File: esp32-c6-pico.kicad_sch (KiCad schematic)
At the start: 52 parts, among them SW1 RESET, SW2 BOOT, U1 ESP32-C6, U3 W25Q32JVZPIQ, U4 SN74LV1T125, Y1 40MHz / CL=8pF

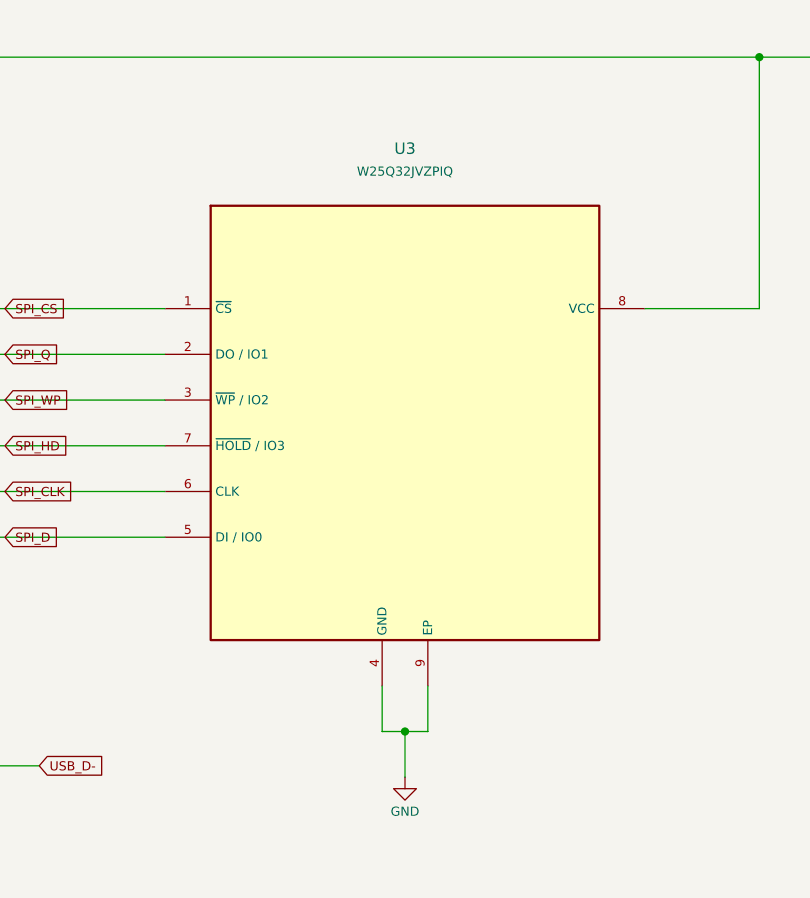
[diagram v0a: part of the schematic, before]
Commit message: Restore SOIC-8 flash, shrink USB diode and remove input fuse
Use W25Q32JVSNIQ in a 150 mil SOIC-8 footprint and BAT760-7 in
SOD-323. Remove F1 and connect USB VBUS directly to the blocking
diode. Preserve the board outline and RF, crystal and USB data routing.

Synchronize schematics, BOM, placement, previews, fabrication notes and
independent checks. ERC, DRC, unconnected items and schematic parity
are all zero. QA passes 45 of 51 checks, retaining six pre-existing failures.
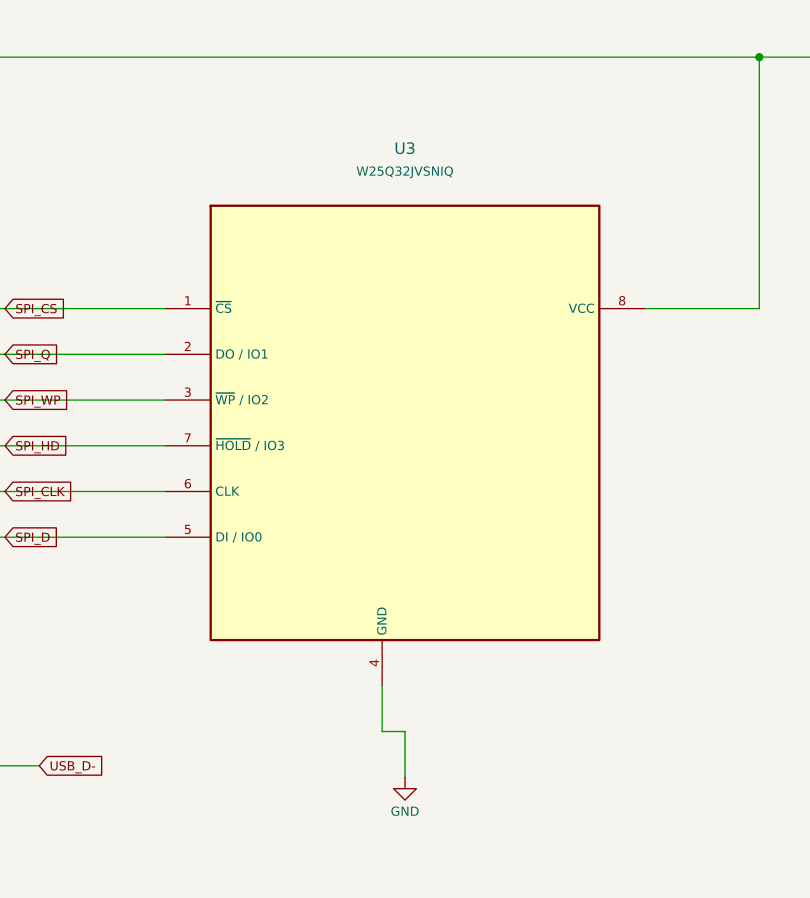
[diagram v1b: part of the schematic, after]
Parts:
- U3: value W25Q32JVZPIQ -> W25Q32JVSNIQ; footprint Package_SON:WSON-8-1EP_6x5mm_P1.27mm_EP3.4x4mm -> Package_SO:SOIC-8_3.9x4.9mm_P1.27mm; symbol Pico_Design:Memory_Flash__W25Q32JVZP -> Pico_Design:Memory_Flash__W25Q32JVSN; AssemblyNote (none) -> SOIC-8 150 mil; 3.9 x 4.9 mm body; no exposed pad; 4 MB, 2.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; MPN W25Q32JVZPIQ -> W25Q32JVSNIQ
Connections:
- net GND: no longer U3.9 (EP)
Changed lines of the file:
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@@
 	)
 	(symbol
-		(lib_id "Pico_Design:Memory_Flash__W25Q32JVZP")
+		(lib_id "Pico_Design:Memory_Flash__W25Q32JVSN")
 		(at 440.69 127 0)
 		(unit 1)
@@
 			)
 		)
-		(property "Value" "W25Q32JVZPIQ"
+		(property "Value" "W25Q32JVSNIQ"
 			(at 440.69 99.06 0)
 			(effects
@@
 			)
 		)
-		(property "Footprint" "Package_SON:WSON-8-1EP_6x5mm_P1.27mm_EP3.4x4mm"
+		(property "Footprint" "Package_SO:SOIC-8_3.9x4.9mm_P1.27mm"
 			(at 440.69 127 0)
 			(effects
@@
 			)
 		)
-		(property "MPN" "W25Q32JVZPIQ"
+		(property "MPN" "W25Q32JVSNIQ"
 			(at 440.69 127 0)
 			(effects
@@
 			)
 		)
-		(property "AssemblyNote" ""
+		(property "AssemblyNote" "SOIC-8 150 mil; 3.9 x 4.9 mm body; no exposed pad; 4 MB, 2.7-3.6 V"
 			(at 440.69 127 0)
 			(effects
@@
 		(pin "8"
 		)
-		(pin "9"
-		)
 		(instances
 			(project "esp32-c6-pico"
@@
 	(wire
 		(pts
-			(xy 440.69 161.29)
-			(xy 443.23 161.29)
-		)
-		(stroke
-			(width 0)
-			(type default)
-		)
-	)
-	(wire
-		(pts
 			(xy 441.96 231.14)
 			(xy 441.96 236.22)
@@
 	(wire
 		(pts
-			(xy 443.23 156.21)
-			(xy 443.23 161.29)
-		)
-		(stroke
-			(width 0)
-			(type default)
-		)
-	)
-	(wire
-		(pts
 			(xy 463.55 67.31)
 			(xy 463.55 72.39)
@@
 		(diameter 0)
 		(color 0 0 0 0)
-	)
-	(junction
-		(at 440.69 161.29)
-		(diameter 0)
-		(color 0 0 0 0)

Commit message: Complete first PCB revision
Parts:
- removed C26: 100nF, Capacitor_SMD:C_0402_1005Metric, symbol Pico_Design:Device__C_Small
- removed C27, C28: DNP, Capacitor_SMD:C_0402_1005Metric, symbol Pico_Design:Device__C_Small
- removed R12, R13: 22R, Resistor_SMD:R_0402_1005Metric, symbol Pico_Design:Device__R_Small
- removed R16: 100k, Resistor_SMD:R_0402_1005Metric, symbol Pico_Design:Device__R_Small
- removed U4: SN74LV1T125, Package_TO_SOT_SMD:SOT-23-5, symbol Pico_Design:Pico_Custom__SN74LV1T125
- added D6: 1N4148WS, Diode_SMD:D_SOD-323, symbol Pico_Design:Device__D
- added R19: 10k, Resistor_SMD:R_0402_1005Metric, symbol Pico_Design:Device__R_Small
- D2: footprint Pico:WS2812B_2020_Compact -> LED_SMD:LED_WS2812B-2020_PLCC4_2.0x2.0mm
- R15: value 330R -> 0R; AssemblyNote (none) -> RGB data series link; 0R per DevKitC-1 v1.4 R17; MPN 330R -> 0R
- R9: value 10k -> 3.3k; AssemblyNote (none) -> GPIO8 strapping pull-up; 3.3k to 3V3 per DevKitC-1 v1.4 R6; MPN 10k -> 3.3k
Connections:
- net USB_MCU_D+ is gone; now on net USB_D+: U1.19 (GPIO13_/_USB_D+)
- net USB_MCU_D- is gone; now on net USB_D-: U1.18 (GPIO12_/_USB_D-)
- net GPIO8: now also D6.1 (K)
- net LED_DATA_5V: now also D6.2 (A), R19.2
- net VBUS_USB: now also R19.1
- net GPIO21_LED renamed GPIO21
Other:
- moved on the sheet: R9
